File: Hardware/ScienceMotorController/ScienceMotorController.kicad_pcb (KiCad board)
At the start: 2 copper layers, 125.7 x 166.4 mm, 155 parts, among them Q1 BSS138, Q2 BSS138, Q3 BSS138, Q4 BSS138, Q5 BSS138, Q6 BSS138, Q7 BSS138, Q8 BSS138, Q9 BSS138, U1 VNH5019A_E, U2 VNH5019A_E, U3 VNH5019A_E, U4 VNH5019A_E, U5 3V3 OKI, U6 TM4C129E_Launchpad, U7 5VA OKI, U8 5VA OKI

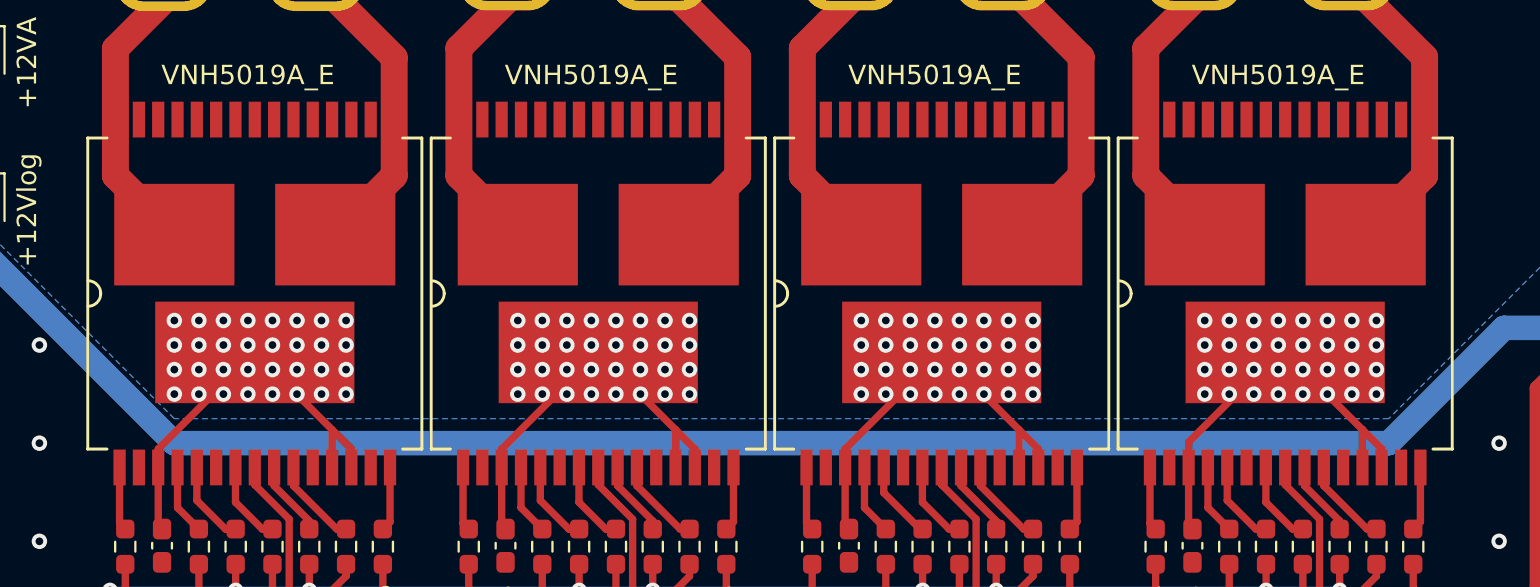
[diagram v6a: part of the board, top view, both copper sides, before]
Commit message: Connected Moco Pads, new Gerbs
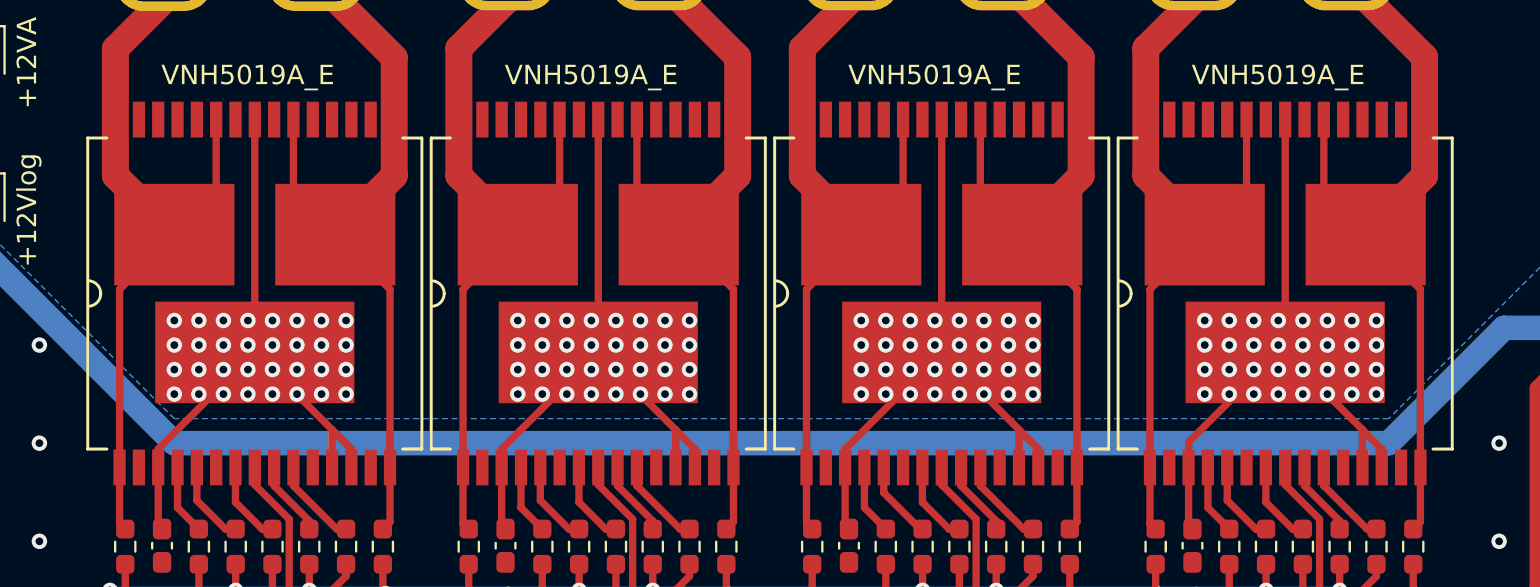
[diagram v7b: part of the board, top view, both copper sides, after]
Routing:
- net +12VA: track 384.2 -> 432.4 mm
- net Net-(Conn4-Pad1): track 18.8 -> 38.8 mm
- net Net-(Conn1-Pad1): track 18.7 -> 38.8 mm
- net Net-(Conn3-Pad1): track 18.8 -> 38.8 mm
- net Net-(Conn2-Pad1): track 18.8 -> 38.8 mm
- net Net-(Conn4-Pad2): track 18.5 -> 38.6 mm
- net Net-(Conn3-Pad2): track 18.5 -> 38.6 mm
- net Net-(Conn2-Pad2): track 18.5 -> 38.6 mm
- net Net-(Conn1-Pad2): track 18.5 -> 38.6 mm

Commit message: Finished schematic and updated footprints
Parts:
- removed AbsEncode5, AbsEncode6: Molex_SL_03, MRDT_Connectors:MOLEX_SL_03_Vertical
- removed C14: 10uF, Capacitor_SMD:C_0603_1608Metric_Pad1.08x0.95mm_HandSolder
- removed D34: LED, LED_SMD:LED_0603_1608Metric_Pad1.05x0.95mm_HandSolder
- removed G***: LOGO, Silkscreens:signature
- removed G***: LOGO, MRDT_Silkscreens:0_MRDT_Logo_50mm
- removed SolVal1, SolVal2, SolVal3, SolVal4, SolVal5, SolVal6, SolVal7, SolVal8, SolVal9: Molex_SL_02, MRDT_Connectors:MOLEX_SL_02_Vertical
- added Conn8: AndersonPP, MRDT_Connectors:Square_Anderson_2_H_Side_By_Side, F.Cu at (186.4, 116.8)
- added DY1: LED, LED_SMD:LED_0603_1608Metric_Pad1.05x0.95mm_HandSolder, F.Cu at (213.2, 58.3)
- added DY10: LED, LED_SMD:LED_0603_1608Metric_Pad1.05x0.95mm_HandSolder, F.Cu at (192.8, 38.8)
- added DY11: LED, LED_SMD:LED_0603_1608Metric_Pad1.05x0.95mm_HandSolder, F.Cu at (217.2, 67.3)
- added DY12: LED, LED_SMD:LED_0603_1608Metric_Pad1.05x0.95mm_HandSolder, F.Cu at (253.9, 156.8)
- added DY2: LED, LED_SMD:LED_0603_1608Metric_Pad1.05x0.95mm_HandSolder, F.Cu at (268.9, 132.6)
- added DY3: LED, LED_SMD:LED_0603_1608Metric_Pad1.05x0.95mm_HandSolder, F.Cu at (270.0, 150.1)
- added DY4: LED, LED_SMD:LED_0603_1608Metric_Pad1.05x0.95mm_HandSolder, F.Cu at (210.6, 62.7)
- added DY5: LED, LED_SMD:LED_0603_1608Metric_Pad1.05x0.95mm_HandSolder, F.Cu at (186.3, 35.3)
- added DY6: LED, LED_SMD:LED_0603_1608Metric_Pad1.05x0.95mm_HandSolder, F.Cu at (251.3, 156.8)
- added DY7: LED, LED_SMD:LED_0603_1608Metric_Pad1.05x0.95mm_HandSolder, F.Cu at (204.1, 52.6)
- added DY8: LED, LED_SMD:LED_0603_1608Metric_Pad1.05x0.95mm_HandSolder, F.Cu at (206.7, 52.6)
- added DY9: LED, LED_SMD:LED_0603_1608Metric_Pad1.05x0.95mm_HandSolder, F.Cu at (262.6, 115.7)
- added J1: RJ45_LED_Shielded, MRDT_Connectors:RJ45_Teensy, F.Cu at (245.1, 135.8)
- added LimSwitch7: Molex_SL_02, MRDT_Connectors:MOLEX_SL_02_Vertical, F.Cu at (257.8, 131.0)
- added LimSwitch8: Molex_SL_02, MRDT_Connectors:MOLEX_SL_02_Vertical, F.Cu at (211.3, 87.3)
- added LimSwitch9: Molex_SL_02, MRDT_Connectors:MOLEX_SL_02_Vertical, F.Cu at (237.7, 112.6)
- added Q10: AO3401A, Package_TO_SOT_SMD:SOT-23, F.Cu at (269.6, 123.9)
- added Q11: SI4156DY, Package_SO:SOIC-8_3.9x4.9mm_P1.27mm, F.Cu at (210.1, 69.1)
- added Q12: SI4156DY, Package_SO:SOIC-8_3.9x4.9mm_P1.27mm, F.Cu at (251.6, 111.8)
- added Q13: SI4156DY, Package_SO:SOIC-8_3.9x4.9mm_P1.27mm, F.Cu at (185.7, 50.2)
- added Q14: SI4156DY, Package_SO:SOIC-8_3.9x4.9mm_P1.27mm, F.Cu at (199.7, 59.1)
- added Q15: SI4156DY, Package_SO:SOIC-8_3.9x4.9mm_P1.27mm, F.Cu at (244.1, 103.2)
- added Q16: SI4156DY, Package_SO:SOIC-8_3.9x4.9mm_P1.27mm, F.Cu at (251.6, 103.3)
- added Q17: SI4156DY, Package_SO:SOIC-8_3.9x4.9mm_P1.27mm, F.Cu at (257.7, 121.2)
- added Q18: SI4156DY, Package_SO:SOIC-8_3.9x4.9mm_P1.27mm, F.Cu at (199.6, 50.6)
- added R59: 120, Resistor_SMD:R_0603_1608Metric_Pad0.98x0.95mm_HandSolder, F.Cu at (252.6, 92.6)
- added R60: 120, Resistor_SMD:R_0603_1608Metric_Pad0.98x0.95mm_HandSolder, F.Cu at (215.8, 58.6)
- added R61: 120, Resistor_SMD:R_0603_1608Metric_Pad0.98x0.95mm_HandSolder, F.Cu at (267.5, 106.1)
- added R62: 120, Resistor_SMD:R_0603_1608Metric_Pad0.98x0.95mm_HandSolder, F.Cu at (238.4, 83.6)
- added R63: 120, Resistor_SMD:R_0603_1608Metric_Pad0.98x0.95mm_HandSolder, F.Cu at (227.3, 66.9)
- added R64: 120, Resistor_SMD:R_0603_1608Metric_Pad0.98x0.95mm_HandSolder, F.Cu at (209.3, 52.7)
- added SW1: SW_Push, Button_Switch_SMD:SW_SPST_EVPBF, F.Cu at (235.7, 120.8)
- added SW10: SW_Push, Button_Switch_SMD:SW_SPST_EVPBF, F.Cu at (268.0, 161.7)
- added SW11: SW_DPDT_x2, Button_Switch_THT:SW_Slide_1P2T_CK_OS102011MS2Q, F.Cu at (253.5, 172.8)
- added SW2: SW_Push, Button_Switch_SMD:SW_SPST_EVPBF, F.Cu at (257.4, 139.1)
- added SW3: SW_Push, Button_Switch_SMD:SW_SPST_EVPBF, F.Cu at (268.0, 171.8)
- added SW4: SW_Push, Button_Switch_SMD:SW_SPST_EVPBF, F.Cu at (249.6, 129.7)
- added SW5: SW_Push, Button_Switch_SMD:SW_SPST_EVPBF, F.Cu at (264.9, 149.2)
- added SW6: SW_Push, Button_Switch_SMD:SW_SPST_EVPBF, F.Cu at (203.1, 85.4)
- added SW7: SW_Push, Button_Switch_SMD:SW_SPST_EVPBF, F.Cu at (257.4, 149.2)
- added SW8: SW_Push, Button_Switch_SMD:SW_SPST_EVPBF, F.Cu at (186.2, 68.1)
- added SW9: SW_Push, Button_Switch_SMD:SW_SPST_EVPBF, F.Cu at (220.2, 109.5)
- added Servo3: Molex_SL_03, MRDT_Connectors:MOLEX_SL_03_Vertical, F.Cu at (187.1, 81.3)
- added Servo4: Molex_SL_03, MRDT_Connectors:MOLEX_SL_03_Vertical, F.Cu at (250.5, 142.9)
- added Servo5: Molex_SL_03, MRDT_Connectors:MOLEX_SL_03_Vertical, F.Cu at (213.3, 100.8)
- added Servo6: Molex_SL_03, MRDT_Connectors:MOLEX_SL_03_Vertical, F.Cu at (221.1, 122.7)
- added U10: IRS2005S, Package_SO:SOIC-8_3.9x4.9mm_P1.27mm, F.Cu at (216.6, 73.8)
- added U11: IRS2005S, Package_SO:SOIC-8_3.9x4.9mm_P1.27mm, F.Cu at (217.6, 82.2)
- added U13: IRS2005S, Package_SO:SOIC-8_3.9x4.9mm_P1.27mm, F.Cu at (236.5, 94.4)
- added U14: IRS2005S, Package_SO:SOIC-8_3.9x4.9mm_P1.27mm, F.Cu at (236.6, 102.9)
- added U9: 74LVC2G04, Package_TO_SOT_SMD:SOT-23-6_Handsoldering, F.Cu at (229.6, 85.1)
- added V1: Via, MRDT_Drill_Holes:4_40_Hole_Corner, F.Cu at (269.7, 143.4)
- added V2: Via, MRDT_Drill_Holes:4_40_Hole_Corner, F.Cu at (198.6, 72.4)
- added V3: Via, MRDT_Drill_Holes:4_40_Hole_Corner, F.Cu at (225.1, 103.7)
- added V4: Via, MRDT_Drill_Holes:4_40_Hole_Corner, F.Cu at (232.6, 113.7)
- C1, C2: value 33nF -> 1u; footprint Capacitor_SMD:C_0603_1608Metric_Pad1.08x0.95mm_HandSolder -> Capacitor_SMD:C_0603_1608Metric
- C10, C9: value 10uF -> 10u; footprint Capacitor_SMD:C_0603_1608Metric_Pad1.08x0.95mm_HandSolder -> Capacitor_SMD:C_0603_1608Metric
- C11, C12, C5, C6, C7, C8: value 10uF -> 1u; footprint Capacitor_SMD:C_0603_1608Metric_Pad1.08x0.95mm_HandSolder -> Capacitor_SMD:C_0603_1608Metric
- C13: value 10uF -> 0.1uF
- C3, C4: value 33nF -> 10u; footprint Capacitor_SMD:C_0603_1608Metric_Pad1.08x0.95mm_HandSolder -> Capacitor_SMD:C_0603_1608Metric
- Conn1: value Motor1 -> Input
- Conn2: value Motor2 -> Output1
- Conn3: value Motor3 -> Output2
- Conn4: value Motor4 -> AndersonPP
- Conn5: value Input -> AndersonPP; footprint MRDT_Connectors:Square_Anderson_3_H_Side_By_Side -> MRDT_Connectors:Square_Anderson_2_H_Side_By_Side; moved to F.Cu
- Conn6: value Output1 -> Molex_SL_02; footprint MRDT_Connectors:Square_Anderson_3_H_Side_By_Side -> MRDT_Connectors:MOLEX_SL_02_Vertical
- Conn7: value Output2 -> AndersonPP
- D1, D14, D15, D17, D18, D2, D23, D24: value LED -> Orange
- D10, D11, D12: value 3.3V -> YELLOW; footprint Diode_SMD:D_0603_1608Metric_Pad1.05x0.95mm_HandSolder -> LED_SMD:LED_0603_1608Metric_Pad1.05x0.95mm_HandSolder
- D13, D25, D26, D27, D28, D29, D30, D31, D32, D33: value LED -> YELLOW
- D16: value LED -> LED(B)
- D19, D20, D21, D22, D3, D4, D8: value LED -> D_Small
- D5, D7: value LED -> GREEN
- D6: value LED -> Green
- D9: value 3.3V -> D_Small; footprint Diode_SMD:D_0603_1608Metric_Pad1.05x0.95mm_HandSolder -> LED_SMD:LED_0603_1608Metric_Pad1.05x0.95mm_HandSolder
- Q1, Q2, Q3, Q4, Q5, Q6, Q7, Q8: value BSS138 -> SI4156DY; footprint Package_TO_SOT_SMD:SOT-23 -> Package_SO:SOIC-8_3.9x4.9mm_P1.27mm
- R1, R2, R34, R35, R36, R54, R55: value 1k -> 4.7k
- R10, R12, R17, R18, R19, R20, R5, R50, R51, R6, R7, R8, R9: value 1k -> 100
- R13, R14, R15, R25, R26, R27: value 3.3k -> 100
- R16, R28: value 3.3k -> 120
- R21: value 10k -> 300
- R22, R23, R24: value 10k -> 100
- R29, R30, R31, R32: value 1.5k -> 120
- R3, R33, R4, R52, R53, R56, R57, R58: value 1k -> 120
- R37: value 130 -> 10k
- R38: value 1k -> 10k
- R40, R41: value 300 -> 4.7k
- R42, R43: value 130 -> 120
- R44, R45, R46, R47, R48, R49: value 130 -> 100
- U1, U2: value VNH5019A_E -> 74LVC2G04; footprint MRDT_ICs:MultiPowerSO_30 -> Package_TO_SOT_SMD:SOT-23-6_Handsoldering
- U3, U4: value VNH5019A_E -> IRS2005S; footprint MRDT_ICs:MultiPowerSO_30 -> Package_SO:SOIC-8_3.9x4.9mm_P1.27mm
- U5: value 3V3 OKI -> TSR_1-2450; footprint MRDT_Devices:OKI_Horizontal -> Converter_DCDC:Converter_DCDC_TRACO_TSR-1_THT
- U6: value TM4C129E_Launchpad -> IRS2005S; footprint MRDT_Shields:TM4C129E_Launchpad_FULL_THT_BOTTOM -> Package_SO:SOIC-8_3.9x4.9mm_P1.27mm
- U7: value 5VA OKI -> IRS2005S; footprint MRDT_Devices:OKI_Horizontal -> Package_SO:SOIC-8_3.9x4.9mm_P1.27mm
- U8: value 5VA OKI -> 74LVC2G04; footprint MRDT_Devices:OKI_Horizontal -> Package_TO_SOT_SMD:SOT-23-6_Handsoldering
- moved U7 239.2 mm to (264.2, 122.1), turned to 90 degrees
- moved U2 231.7 mm to (252.3, 161.9)
- moved D20 229.1 mm to (267.7, 114.8)
- moved D22 227.9 mm to (270.0, 154.5)
- moved D14 227.1 mm to (256.1, 101.9), turned to 90 degrees
- moved R30 226.6 mm to (270.3, 114.9), turned to 90 degrees
- moved D10 221.8 mm to (265.1, 115.7), turned to 90 degrees
- moved Conn2 221.4 mm to (237.1, 147.6), turned to 90 degrees
- moved C1 218.9 mm to (251.3, 148.2), turned to 90 degrees
- moved D16 218.9 mm to (256.1, 106.3), turned to 90 degrees
- moved R33 212.7 mm to (265.0, 106.9), turned to 90 degrees
- moved R31 212.3 mm to (261.2, 102.0), turned to 90 degrees
- moved D11 211.9 mm to (251.3, 152.4), turned to 90 degrees
- moved C6 209.7 mm to (270.2, 106.4), turned to 90 degrees
- moved C4 209.2 mm to (261.3, 97.8), turned to 90 degrees
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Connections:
- AbsEncode1 pad 1: +3V3 -> GND
- AbsEncode1 pad 2: GND -> Encoder_PWM_1
- AbsEncode1 pad 3: Encoder_PWM_1 -> +5V
- AbsEncode2 pad 1: +3V3 -> GND
- AbsEncode2 pad 2: GND -> Encoder_PWM_2
- AbsEncode2 pad 3: Encoder_PWM_4 -> +5V
- AbsEncode3 pad 1: +3V3 -> GND
- AbsEncode3 pad 2: GND -> Encoder_PWM_3
- AbsEncode3 pad 3: Encoder_PWM_2 -> +5V
- AbsEncode4 pad 1: +3V3 -> GND
- AbsEncode4 pad 2: GND -> Encoder_PWM_4
- AbsEncode4 pad 3: Encoder_PWM_5 -> +5V
- C1 pad 1: Current_Sense_1 -> Net-(C1-Pad1)
- C1 pad 2: GND -> /M4+
- C10 pad 1: +3V3 -> /M4+
- C10 pad 2: GND -> /M4-
- C11 pad 1: +12VA -> Net-(C11-Pad1)
- C11 pad 2: GND -> /M4-
- C12 pad 1: +5VA -> Net-(C12-Pad1)
- C12 pad 2: GND -> /M4-
- C13 pad 1: +12VA -> Net-(C13-Pad1)
- C2 pad 1: Current_Sense_2 -> Net-(C2-Pad1)
- C2 pad 2: GND -> /M4+
- C3 pad 1: Current_Sense_3 -> /M4+
- C3 pad 2: GND -> /M4-
- C4 pad 1: Current_Sense_4 -> /M4+
- C4 pad 2: GND -> /M4-
- C5 pad 1: +12VA -> Net-(C5-Pad1)
- C5 pad 2: GND -> /M4-
- C6 pad 1: +12VA -> Net-(C6-Pad1)
- C6 pad 2: GND -> /M4-
- C7 pad 1: +12VA -> Net-(C7-Pad1)
- C7 pad 2: GND -> /M4+
- C8 pad 1: +12VA -> Net-(C8-Pad1)
- C8 pad 2: GND -> /M4+
- C9 pad 1: +12V -> /M4+
- C9 pad 2: GND -> /M4-
- Conn1 pad 1: Net-(Conn1-Pad1) -> GND
- Conn1 pad 2: Net-(Conn1-Pad2) -> +12V
- Conn2 pad 1: Net-(Conn2-Pad1) -> GND
- Conn2 pad 2: Net-(Conn2-Pad2) -> +12V
- Conn3 pad 1: Net-(Conn3-Pad1) -> GND
- Conn3 pad 2: Net-(Conn3-Pad2) -> +12V
- Conn4 pad 1: Net-(Conn4-Pad1) -> /M4+
- Conn4 pad 2: Net-(Conn4-Pad2) -> /M4-
- Conn5 pad 1: GND -> /M4+
- Conn5 pad 2: +12V -> /M4-
- Conn6 pad 1: GND -> Net-(Conn6-Pad1)
- Conn6 pad 2: +12V -> GND
- Conn7 pad 1: GND -> /M4+
- Conn7 pad 2: +12V -> /M4-
- D1 pad 1: GND -> Net-(D1-Pad1)
- D1 pad 2: Net-(D1-Pad2) -> FWD_PWM_2
- D10 pad 1: Current_Sense_2 -> GND
- D10 pad 2: GND -> Net-(D10-Pad2)
- D11 pad 1: Current_Sense_3 -> GND
- D11 pad 2: GND -> Net-(D11-Pad2)
- D12 pad 1: Current_Sense_4 -> GND
- D12 pad 2: GND -> Net-(D12-Pad2)
- D14 pad 1: GND -> Net-(D14-Pad1)
- D14 pad 2: Net-(D14-Pad2) -> RVS_PWM_2
- D15 pad 1: GND -> Net-(D15-Pad1)
- D15 pad 2: Net-(D15-Pad2) -> RVS_PWM_1
- D17 pad 1: GND -> Net-(D17-Pad1)
- D17 pad 2: Net-(D17-Pad2) -> FWD_PWM_5
- D18 pad 1: GND -> Net-(D18-Pad1)
- D18 pad 2: Net-(D18-Pad2) -> FWD_PWM_3
- D19 pad 1: GND -> Net-(C7-Pad1)
- D19 pad 2: Net-(D19-Pad2) -> +12V
- D2 pad 1: GND -> Net-(D2-Pad1)
- D2 pad 2: Net-(D2-Pad2) -> FWD_PWM_1
- D20 pad 1: GND -> Net-(C8-Pad1)
- D20 pad 2: Net-(D20-Pad2) -> +12V
- D21 pad 1: GND -> Net-(C11-Pad1)
- D21 pad 2: Net-(D21-Pad2) -> +12V
- D22 pad 1: GND -> Net-(C12-Pad1)
- D22 pad 2: Net-(D22-Pad2) -> +12V
- D23 pad 1: GND -> Net-(D23-Pad1)
- D23 pad 2: Net-(D23-Pad2) -> RVS_PWM_5
- D24 pad 2: +12VA -> RVS_PWM_3
- D25 pad 1: Net-(D25-Pad1) -> GND
- D25 pad 2: +12VA -> Net-(D25-Pad2)
- D26 pad 1: Net-(D26-Pad1) -> GND
- D26 pad 2: +12VA -> Net-(D26-Pad2)
- D27 pad 1: Net-(D27-Pad1) -> GND
- D27 pad 2: +12VA -> Net-(D27-Pad2)
- D28 pad 1: Net-(D28-Pad1) -> GND
- D28 pad 2: +12VA -> Net-(D28-Pad2)
- D29 pad 1: Net-(D29-Pad1) -> GND
- D29 pad 2: +12VA -> Net-(D29-Pad2)
- D3 pad 1: GND -> Net-(C1-Pad1)
- D3 pad 2: Net-(D3-Pad2) -> +12V
- D30 pad 1: Net-(D30-Pad1) -> GND
- D30 pad 2: +12VA -> Net-(D30-Pad2)
- D31 pad 1: Net-(D31-Pad1) -> GND
- D31 pad 2: +12VA -> Net-(D31-Pad2)
- D32 pad 1: Net-(D32-Pad1) -> GND
- D32 pad 2: +12VA -> Net-(D32-Pad2)
- D4 pad 1: GND -> Net-(C2-Pad1)
- D4 pad 2: Net-(D4-Pad2) -> +12V
- D8 pad 1: GND -> Net-(C5-Pad1)
- D8 pad 2: Net-(D8-Pad2) -> +12V
- D9 pad 1: Current_Sense_1 -> Net-(C6-Pad1)
- D9 pad 2: GND -> +12V
- LimSwitch2 pad 2: Limit_Switch_4 -> Limit_Switch_3
- LimSwitch3 pad 2: Limit_Switch_2 -> Limit_Switch_9
- LimSwitch4 pad 2: Limit_Switch_5 -> Limit_Switch_4
- LimSwitch5 pad 2: Limit_Switch_3 -> Limit_Switch_5
- LimSwitch6 pad 2: Limit_Switch_6 -> Limit_Switch_7
- Q1 pad 1: Solenoid_Valve_1 -> /M4+
- Q1 pad 2: GND -> /M4+
- Q1 pad 3: Net-(Q1-Pad3) -> /M4+
- Q2 pad 1: Solenoid_Valve_2 -> GND
- Q2 pad 3: Net-(Q2-Pad3) -> GND
- Q3 pad 1: Solenoid_Valve_3 -> /M4+
- Q3 pad 2: GND -> /M4+
- Q3 pad 3: Net-(Q3-Pad3) -> /M4+
- Q4 pad 1: Solenoid_Valve_4 -> GND
- Q4 pad 3: Net-(Q4-Pad3) -> GND
- Q5 pad 1: Solenoid_Valve_5 -> /M4-
- Q5 pad 2: GND -> /M4-
- Q5 pad 3: Net-(Q5-Pad3) -> /M4-
- Q6 pad 1: Solenoid_Valve_6 -> GND
- Q6 pad 3: Net-(Q6-Pad3) -> GND
- Q7 pad 1: Solenoid_Valve_7 -> /M4-
- Q7 pad 2: GND -> /M4-
- Q7 pad 3: Net-(Q7-Pad3) -> /M4-
- Q8 pad 1: Solenoid_Valve_8 -> GND
- Q8 pad 3: Net-(Q8-Pad3) -> GND
- Q9 pad 1: Solenoid_Valve_9 -> Peristaltic Pump
- R1 pad 1: Net-(D1-Pad2) -> FWD_PWM_2
- R1 pad 2: Net-(Conn1-Pad2) -> GND
- R10 pad 1: Net-(R10-Pad1) -> Net-(DY6-Pad2)
- R10 pad 2: INA_2 -> Servo_6_SW
- R11 pad 1: Net-(R11-Pad1) -> Net-(D5-Pad2)
- R11 pad 2: INA_3 -> +12V
- R12 pad 2: INA_4 -> Net-(Q1-Pad4)
- R13 pad 2: +3V3 -> Net-(Q2-Pad4)
- R14 pad 2: +3V3 -> Net-(Q3-Pad4)
- R15 pad 2: +3V3 -> Net-(Q4-Pad4)
- R16 pad 1: Net-(R16-Pad1) -> +3V3
- R16 pad 2: +3V3 -> Net-(D6-Pad2)
- R17 pad 1: Net-(R17-Pad1) -> Net-(DY7-Pad2)
- R17 pad 2: PWM_1 -> Motor_1_SW
- R18 pad 1: Net-(R18-Pad1) -> Net-(DY8-Pad2)
- R18 pad 2: PWM_2 -> Motor_2_SW
- R19 pad 1: Net-(R19-Pad1) -> Net-(DY9-Pad2)
- R19 pad 2: PWM_3 -> Motor_3_SW
- R2 pad 1: Net-(D2-Pad2) -> FWD_PWM_1
- R2 pad 2: Net-(Conn2-Pad2) -> GND
- R20 pad 1: Net-(R20-Pad1) -> Net-(DY10-Pad2)
- R20 pad 2: PWM_4 -> Motor_4_SW
- R21 pad 1: Net-(R21-Pad1) -> +5V
- R21 pad 2: Current_Sense_1 -> Net-(D7-Pad2)
- R22 pad 2: Current_Sense_2 -> Net-(Q5-Pad4)
- R23 pad 2: Current_Sense_3 -> Net-(Q6-Pad4)
- R24 pad 2: Current_Sense_4 -> Net-(Q7-Pad4)
- R25 pad 2: +3V3 -> Net-(Q8-Pad4)
- R26 pad 1: Net-(R26-Pad1) -> Net-(DY11-Pad2)
- R26 pad 2: +3V3 -> Manual_Control_Left
- R27 pad 1: Net-(R27-Pad1) -> Net-(DY12-Pad2)
- R27 pad 2: +3V3 -> Manual_Control_Right
- R28 pad 1: Net-(R28-Pad1) -> Encoder_PWM_1
- R28 pad 2: +3V3 -> Net-(D10-Pad2)
- R29 pad 1: Net-(R21-Pad1) -> Encoder_PWM_2
- R29 pad 2: GND -> Net-(D11-Pad2)
- R3 pad 1: Net-(D3-Pad2) -> Net-(D1-Pad1)
- R3 pad 2: Net-(Conn3-Pad2) -> GND
- R30 pad 1: Net-(R22-Pad1) -> Encoder_PWM_3
- R30 pad 2: GND -> Net-(D12-Pad2)
- R31 pad 1: Net-(R23-Pad1) -> Encoder_PWM_4
- R31 pad 2: GND -> Net-(D13-Pad2)
- R32 pad 1: Net-(R24-Pad1) -> GND
- R32 pad 2: GND -> Net-(D14-Pad1)
- R33 pad 1: Net-(R33-Pad1) -> GND
- R33 pad 2: INB_1 -> Net-(D15-Pad1)
- R34 pad 1: Net-(R34-Pad1) -> RVS_PWM_2
- R34 pad 2: INB_2 -> GND
- R35 pad 1: Net-(R35-Pad1) -> RVS_PWM_1
- R35 pad 2: INB_3 -> GND
- R36 pad 1: Net-(R36-Pad1) -> Peristaltic Pump
- R36 pad 2: INB_4 -> GND
- R37 pad 1: Net-(D13-Pad2) -> +12V
- R37 pad 2: +3V3 -> Net-(Q10-Pad1)
- R38 pad 1: Net-(D14-Pad2) -> Net-(Q10-Pad1)
- R38 pad 2: +12V -> Net-(Q9-Pad3)
- R39 pad 1: Net-(D15-Pad2) -> Net-(D16-Pad2)
- R39 pad 2: +12VA -> Net-(Conn6-Pad1)
- R4 pad 1: Net-(D4-Pad2) -> Net-(D2-Pad1)
- R4 pad 2: Net-(Conn4-Pad2) -> GND
- R40 pad 1: Net-(D16-Pad2) -> FWD_PWM_5
- R40 pad 2: +5VA -> GND
- R41 pad 1: Net-(D17-Pad2) -> FWD_PWM_3
- R41 pad 2: +5VA -> GND
- R42 pad 1: Net-(R42-Pad1) -> Net-(D17-Pad1)
- R42 pad 2: Net-(D18-Pad2) -> GND
- R43 pad 1: Net-(D19-Pad2) -> Net-(D18-Pad1)
- R43 pad 2: Net-(R43-Pad2) -> GND
- R44 pad 1: Net-(D20-Pad2) -> Net-(R44-Pad1)
- R44 pad 2: Limit_Switch_1 -> Net-(Q11-Pad4)
- R45 pad 1: Net-(D21-Pad2) -> Net-(R45-Pad1)
- R45 pad 2: Limit_Switch_4 -> Net-(Q12-Pad4)
- R46 pad 1: Net-(D22-Pad2) -> Net-(R46-Pad1)
- R46 pad 2: Limit_Switch_2 -> Net-(Q13-Pad4)
- R47 pad 1: Net-(D23-Pad2) -> Net-(R47-Pad1)
- R47 pad 2: Limit_Switch_5 -> Net-(Q14-Pad4)
- R48 pad 1: Net-(D33-Pad2) -> Net-(R48-Pad1)
- R48 pad 2: Limit_Switch_3 -> Net-(Q15-Pad4)
- R49 pad 2: Limit_Switch_6 -> Net-(Q16-Pad4)
- R5 pad 1: Net-(D5-Pad2) -> Net-(DY1-Pad2)
- R5 pad 2: Net-(Conn1-Pad1) -> Servo_1_SW
- R50 pad 1: Net-(D24-Pad1) -> Net-(R50-Pad1)
- R50 pad 2: Net-(Q1-Pad3) -> Net-(Q17-Pad4)
- R51 pad 1: Net-(D25-Pad1) -> Net-(R51-Pad1)
- R51 pad 2: Net-(Q2-Pad3) -> Net-(Q18-Pad4)
- R52 pad 1: Net-(D26-Pad1) -> GND
- R52 pad 2: Net-(Q3-Pad3) -> Net-(D23-Pad1)
- R53 pad 1: Net-(D27-Pad1) -> GND
- R53 pad 2: Net-(Q4-Pad3) -> Net-(D24-Pad1)
- R54 pad 1: Net-(D28-Pad1) -> RVS_PWM_5
- R54 pad 2: Net-(Q5-Pad3) -> GND
- R55 pad 1: Net-(D29-Pad1) -> RVS_PWM_3
- R55 pad 2: Net-(Q6-Pad3) -> GND
- R56 pad 1: Net-(D30-Pad1) -> Net-(D25-Pad2)
- R56 pad 2: Net-(Q7-Pad3) -> Limit_Switch_1
- R57 pad 1: Net-(D31-Pad1) -> Net-(D26-Pad2)
- R57 pad 2: Net-(Q8-Pad3) -> Limit_Switch_3
- R58 pad 1: Net-(D32-Pad1) -> Net-(D27-Pad2)
- R58 pad 2: Net-(Q9-Pad3) -> Limit_Switch_9
- R6 pad 1: Net-(D6-Pad2) -> Net-(DY2-Pad2)
- R6 pad 2: Net-(Conn2-Pad1) -> Servo_2_SW
- R7 pad 1: Net-(D7-Pad2) -> Net-(DY3-Pad2)
- R7 pad 2: Net-(Conn3-Pad1) -> Servo_3_SW
- R8 pad 1: Net-(D8-Pad2) -> Net-(DY4-Pad2)
- R8 pad 2: Net-(Conn4-Pad1) -> Servo_4_SW
- R9 pad 1: Net-(R9-Pad1) -> Net-(DY5-Pad2)
- R9 pad 2: INA_1 -> Servo_5_SW
- Servo1 pad 1: +5VA -> +5V
- Servo1 pad 3: Servo_1 -> Servo_6
- Servo2 pad 1: +5VA -> +5V
- U1 pad 1: Net-(Conn1-Pad2) -> FWD_PWM_2
- U1 pad 2: Net-(U1-Pad2) -> GND
- U1 pad 3: +12VA -> RVS_PWM_2
- U1 pad 4: Net-(R9-Pad1) -> Net-(U1-Pad4)
- U1 pad 5: Net-(R13-Pad1) -> +3V3
- U2 pad 1: Net-(Conn2-Pad2) -> FWD_PWM_1
- U2 pad 2: Net-(U2-Pad2) -> GND
- U2 pad 3: +12VA -> RVS_PWM_1
- U2 pad 4: Net-(R10-Pad1) -> Net-(U2-Pad4)
- U2 pad 5: Net-(R14-Pad1) -> +3V3
- U3 pad 1: Net-(Conn3-Pad2) -> +12V
- U3 pad 2: Net-(U3-Pad2) -> FWD_PWM_2
- U3 pad 3: +12VA -> Net-(U1-Pad6)
- U3 pad 4: Net-(R11-Pad1) -> GND
- U3 pad 5: Net-(R15-Pad1) -> Net-(R13-Pad1)
- U3 pad 6: Net-(U3-Pad6) -> /M4+
- U3 pad 7: Net-(R19-Pad1) -> Net-(R12-Pad1)
- U3 pad 8: Net-(R23-Pad1) -> Net-(C1-Pad1)
- U4 pad 1: Net-(Conn4-Pad2) -> +12V
- U4 pad 2: Net-(U4-Pad2) -> FWD_PWM_1
- U4 pad 3: +12VA -> Net-(U2-Pad6)
- U4 pad 4: Net-(R12-Pad1) -> GND
- U4 pad 5: Net-(R16-Pad1) -> Net-(R15-Pad1)
- U4 pad 6: Net-(U4-Pad6) -> /M4+
- U4 pad 7: Net-(R20-Pad1) -> Net-(R14-Pad1)
- U4 pad 8: Net-(R24-Pad1) -> Net-(C2-Pad1)
- U5 pad 3: +3V3 -> +5V
- U7 pad 1: +12VA -> +12V
- U7 pad 2: GND -> RVS_PWM_1
- U7 pad 3: +5VA -> Net-(U2-Pad4)
- U8 pad 1: +12VA -> FWD_PWM_5
- U8 pad 3: +5VA -> RVS_PWM_5
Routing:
- net +12VA: track 432.4 -> 0.00 mm, vias 128 -> 0
- net +3V3: track 324.8 -> 0.00 mm, vias 10 -> 0
- net Net-(R24-Pad1): track 140.5 -> 0.00 mm
- net +12V: track 138.6 -> 0.00 mm
- net INB_4: track 136.4 -> 0.00 mm, vias 1 -> 0
- net INA_4: track 131.6 -> 0.00 mm, vias 1 -> 0
- net Net-(R23-Pad1): track 127.9 -> 0.00 mm
- net PWM_3: track 120.7 -> 0.00 mm, vias 1 -> 0
- net PWM_4: track 119.9 -> 0.00 mm, vias 1 -> 0
- net INB_3: track 118.0 -> 0.00 mm, vias 1 -> 0
- net Net-(R22-Pad1): track 115.4 -> 0.00 mm
- net Encoder_PWM_4: track 113.2 -> 0.00 mm
- net Net-(R21-Pad1): track 111.4 -> 0.00 mm
- net Solenoid_Valve_1: track 110.7 -> 0.00 mm
- net INA_3: track 109.6 -> 0.00 mm, vias 1 -> 0
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- removed copper zone on B.Cu, net +12VA
- removed copper zone on B.Cu, net GND
- removed copper zone on F.Cu, net GND
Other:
- net class Default removed
- board text removed: "+12VA"
- board text removed: "+12Vlog"
- board text removed: "Encoder 1"
- board text removed: "Encoder 2"
- board text removed: "Encoder 3"
- board text removed: "Encoder 4"
- board text removed: "Encoder 5"
- board text removed: "Encoder 6"
- board text removed: "Limit 1"
- board text removed: "Limit 2"
- board text removed: "Limit 3"
- board text removed: "Limit 4"
- board text removed: "Limit 5"
- board text removed: "Limit 6"
- board text removed: "Motor 1"
- board text removed: "Motor 2"
- board text removed: "Motor 3"
- board text removed: "Motor 4"
- board text removed: "Out A"
- board text removed: "Out B"
- board text removed: "Power In"
- board text removed: "Power Out"
- board text removed: "Power Out Logic Only"
- board text removed: "Science Motor Controller Board, Rev 2 Mars Rover Design Team Missouri S&T, 2022 Robert Squires"
- board text removed: "Servo 1"
- board text removed: "Servo 2"
- board text removed: "Solenoid 1"
- board text removed: "Solenoid 2"
- board text removed: "Solenoid 3"
- board text removed: "Solenoid 4"
- board text removed: "Solenoid 5"
- board text removed: "Solenoid 6"
- board text removed: "Solenoid 7"
- board text removed: "Solenoid 8"
- board text removed: "Solenoid 9"
